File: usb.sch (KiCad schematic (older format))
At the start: 37 parts, among them J12 SM05B-SRSS-TB, J16 SM05B-SRSS-TB, J4 SM05B-SRSS-TB, J8 SM05B-SRSS-TB, U1 USB4715, U10 TPS2054BDR, U9 MIC803-30D4VM3-TR, X1 ASCO

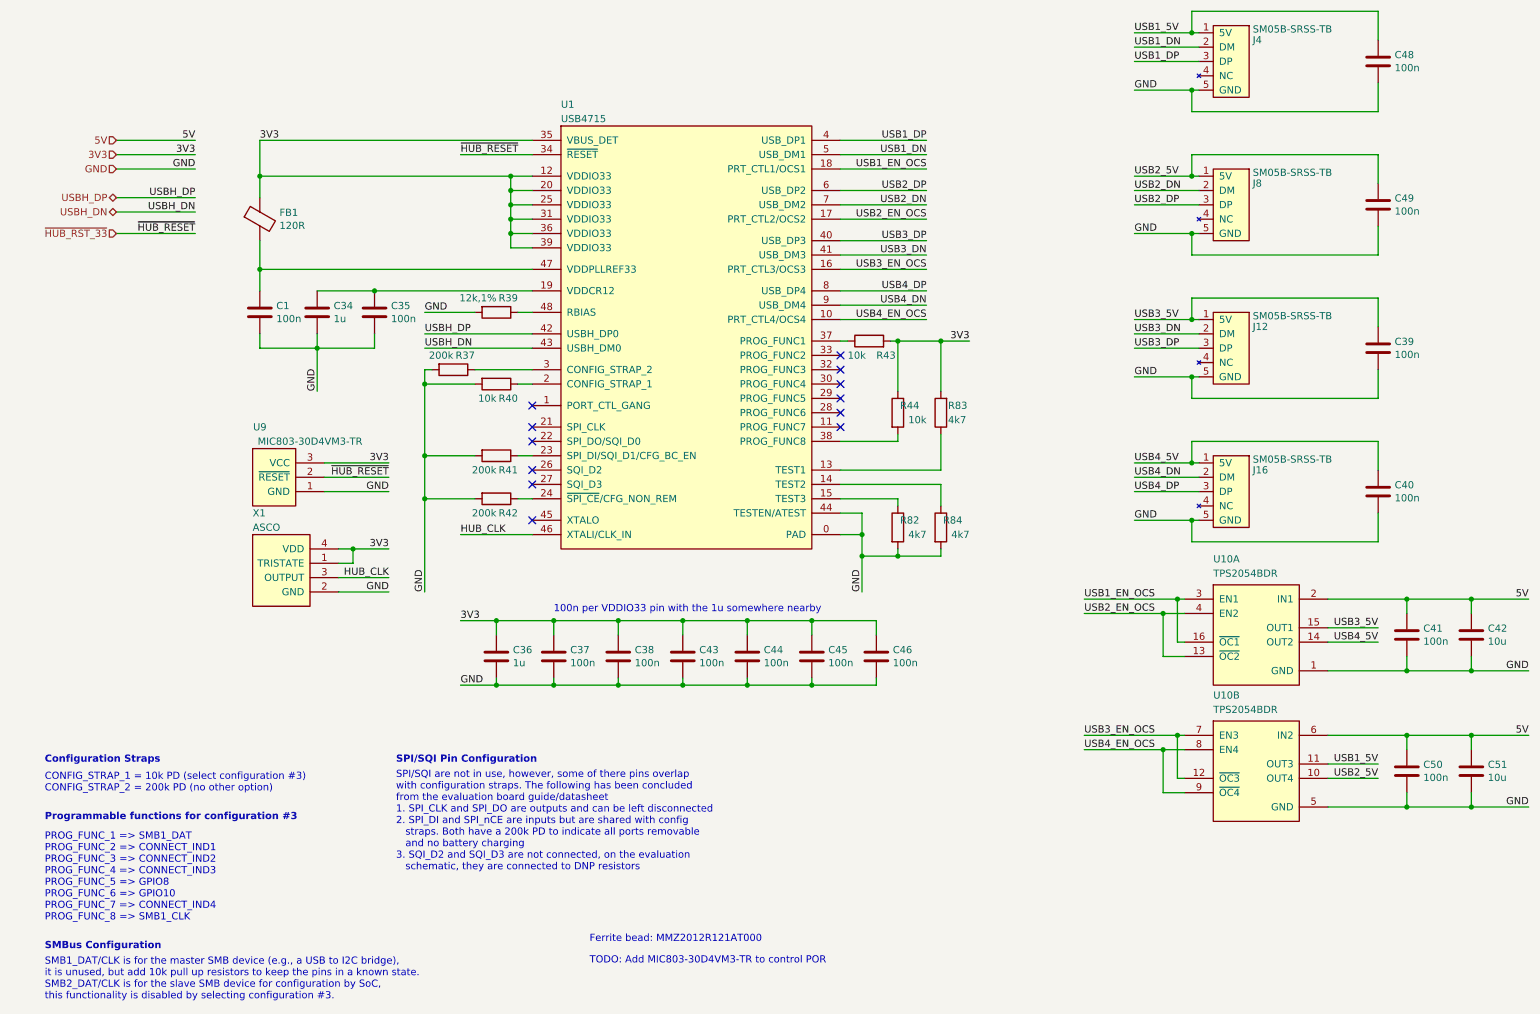
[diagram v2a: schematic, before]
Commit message: Route remaining connections. Check schematics for errors.
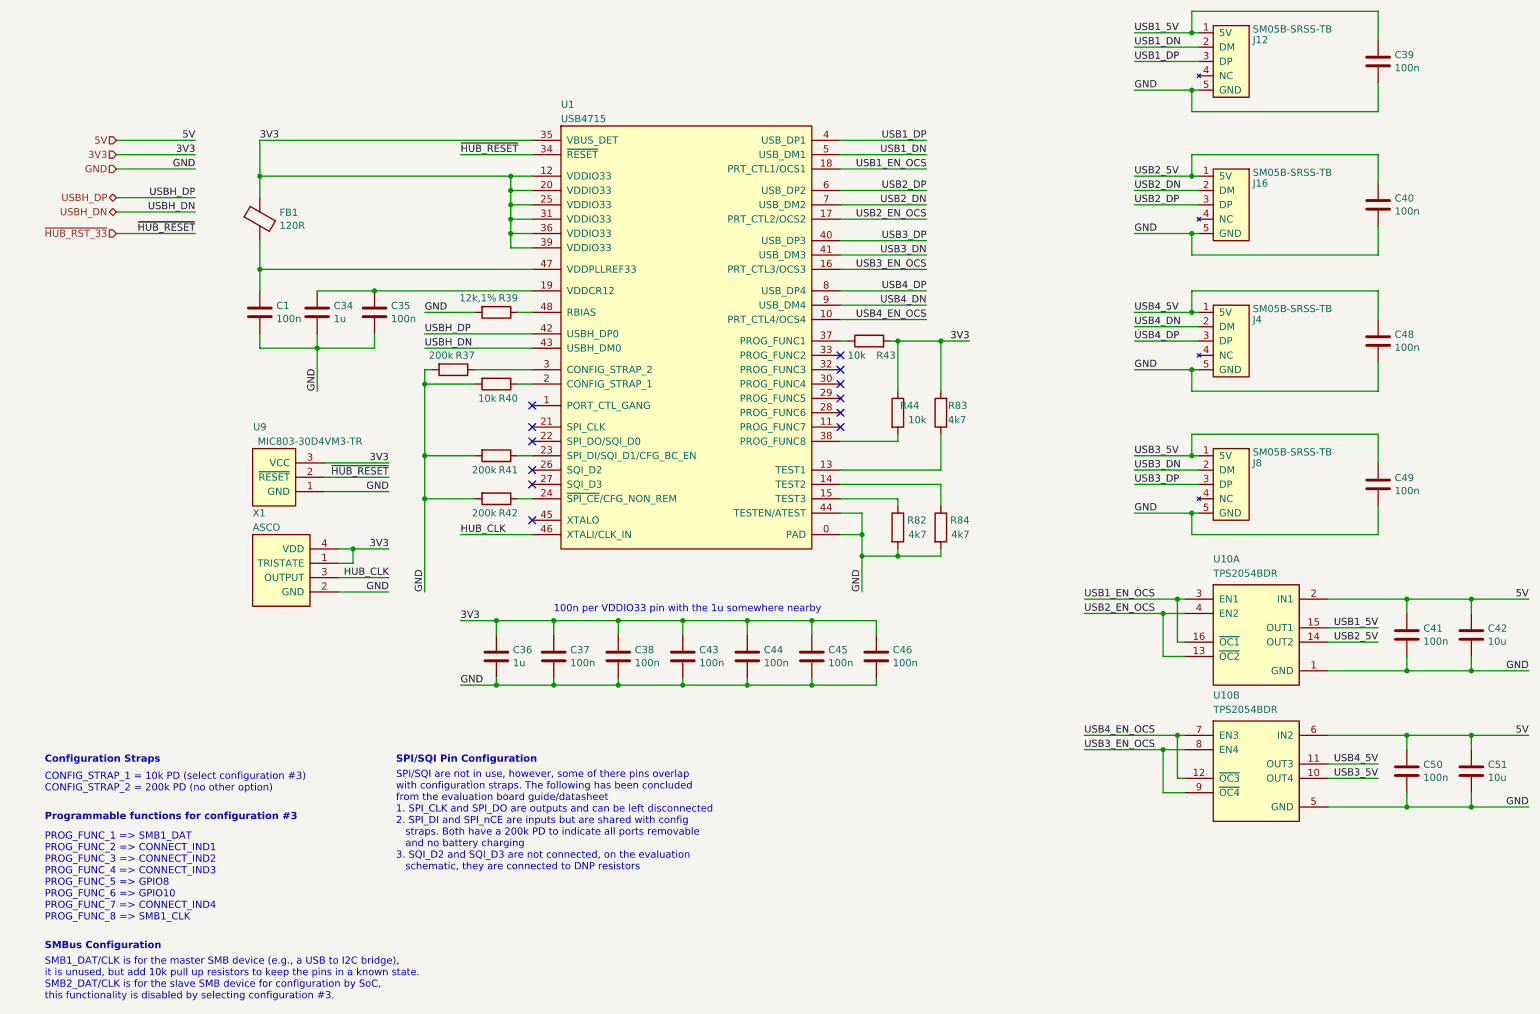
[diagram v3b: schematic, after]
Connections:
- net USB1_5V: now also C39.1, J12.1 (5V), U10.15 (OUT1); no longer C48.1, J4.1 (5V), U10.11 (OUT3)
- net USB1_DN: now also J12.2 (DM); no longer J4.2 (DM)
- net USB1_DP: now also J12.3 (DP); no longer J4.3 (DP)
- net USB2_5V: now also C40.1, J16.1 (5V), U10.14 (OUT2); no longer C49.1, J8.1 (5V), U10.10 (OUT4)
- net USB2_DN: now also J16.2 (DM); no longer J8.2 (DM)
- net USB2_DP: now also J16.3 (DP); no longer J8.3 (DP)
- net USB3_5V: now also C49.1, J8.1 (5V), U10.10 (OUT4); no longer C39.1, J12.1 (5V), U10.15 (OUT1)
- net USB3_DN: now also J8.2 (DM); no longer J12.2 (DM)
- net USB3_DP: now also J8.3 (DP); no longer J12.3 (DP)
- net USB3_EN_OCS: now also U10.8 (EN4), U10.9 (~OC4); no longer U10.12 (~OC3), U10.7 (EN3)
- net USB4_5V: now also C48.1, J4.1 (5V), U10.11 (OUT3); no longer C40.1, J16.1 (5V), U10.14 (OUT2)
- net USB4_DN: now also J4.2 (DM); no longer J16.2 (DM)
- net USB4_DP: now also J4.3 (DP); no longer J16.3 (DP)
- net USB4_EN_OCS: now also U10.12 (~OC3), U10.7 (EN3); no longer U10.8 (EN4), U10.9 (~OC4)
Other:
- note removed: "Ferrite bead: MMZ2012R121AT000"
- note removed: "TODO: Add MIC803-30D4VM3-TR to control POR"
- moved on the sheet: C39, C40, C48, C49, J12, J16, J4, J8
